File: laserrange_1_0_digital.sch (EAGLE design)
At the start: 32 parts, among them U1 STM32F10XRXT6

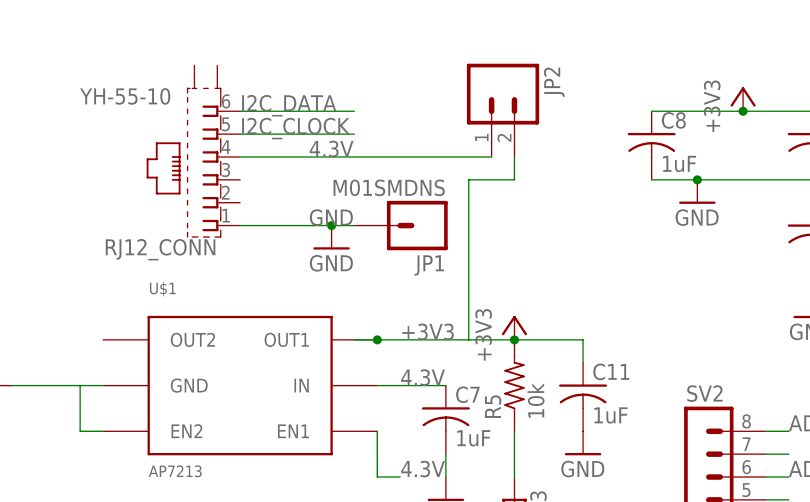
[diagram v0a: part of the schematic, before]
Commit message: Fixed the RJ12 connector footpad connections
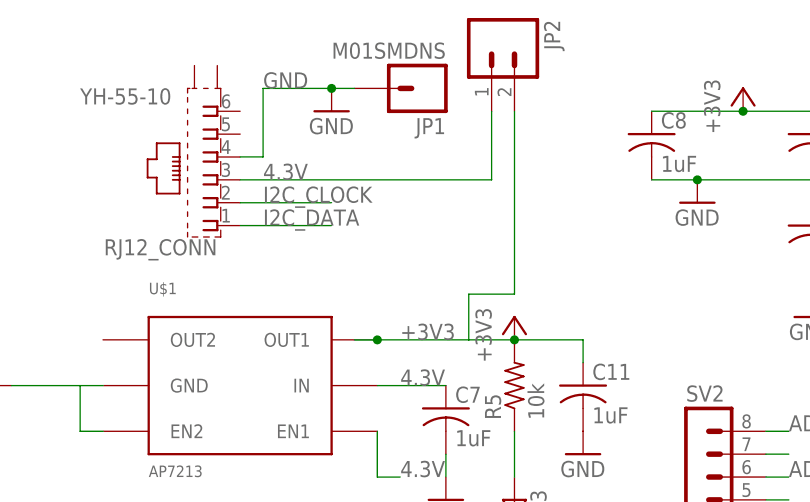
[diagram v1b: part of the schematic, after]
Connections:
- net 4.3V: now also RJ12_CONN.3; no longer RJ12_CONN.4
- net GND: now also RJ12_CONN.4; no longer RJ12_CONN.1
- net I2C_CLOCK: now also RJ12_CONN.2; no longer RJ12_CONN.5
- net I2C_DATA: now also RJ12_CONN.1; no longer RJ12_CONN.6
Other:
- moved on the sheet: JP1, JP2
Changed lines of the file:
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@@
 <instance part="GND6" gate="1" x="114.3" y="-25.4"/>
 <instance part="GND7" gate="1" x="25.4" y="55.88"/>
-<instance part="GND8" gate="1" x="-15.24" y="50.8"/>
+<instance part="GND8" gate="1" x="-15.24" y="66.04"/>
 <instance part="GND2" gate="1" x="5.08" y="0" rot="R90"/>
 <instance part="GND9" gate="1" x="53.34" y="66.04" rot="R270"/>
@@
 <instance part="R9" gate="G$1" x="157.48" y="-5.08"/>
 <instance part="GND15" gate="1" x="167.64" y="0"/>
-<instance part="JP2" gate="G$1" x="2.54" y="68.58" rot="R270"/>
-<instance part="JP1" gate="G$1" x="-5.08" y="53.34" rot="R180"/>
+<instance part="JP2" gate="G$1" x="2.54" y="73.66" rot="R270"/>
+<instance part="JP1" gate="G$1" x="-5.08" y="68.58" rot="R180"/>
 </instances>
 <busses>
@@
 <net name="4.3V" class="0">
 <segment>
-<label x="-17.78" y="60.96" size="1.778" layer="95"/>
-<pinref part="RJ12_CONN" gate="G$1" pin="4"/>
-<wire x1="2.54" y1="60.96" x2="-25.4" y2="60.96" width="0.1524" layer="91"/>
-<pinref part="JP2" gate="G$1" pin="1"/>
-</segment>
-<segment>
 <pinref part="U$1" gate="G$1" pin="IN"/>
 <wire x1="-10.16" y1="35.56" x2="-2.54" y2="35.56" width="0.1524" layer="91"/>
@@
 <label x="-7.62" y="25.4" size="1.778" layer="95"/>
 </segment>
+<segment>
+<pinref part="JP2" gate="G$1" pin="1"/>
+<wire x1="2.54" y1="66.04" x2="2.54" y2="58.42" width="0.1524" layer="91"/>
+<pinref part="RJ12_CONN" gate="G$1" pin="3"/>
+<wire x1="2.54" y1="58.42" x2="-25.4" y2="58.42" width="0.1524" layer="91"/>
+<label x="-22.86" y="58.42" size="1.778" layer="95"/>
+</segment>
 </net>
 <net name="I2C_CLOCK" class="0">
-<segment>
-<wire x1="-25.4" y1="63.5" x2="-12.7" y2="63.5" width="0.1524" layer="91"/>
-<label x="-25.4" y="63.5" size="1.778" layer="95"/>
-<pinref part="RJ12_CONN" gate="G$1" pin="5"/>
-</segment>
 <segment>
 <pinref part="U1" gate="PORTB_L" pin="PB6"/>
@@
 <label x="165.1" y="50.8" size="1.778" layer="95"/>
 </segment>
+<segment>
+<pinref part="RJ12_CONN" gate="G$1" pin="2"/>
+<wire x1="-25.4" y1="55.88" x2="-15.24" y2="55.88" width="0.1524" layer="91"/>
+<label x="-22.86" y="55.88" size="1.778" layer="95"/>
+</segment>
 </net>
 <net name="I2C_DATA" class="0">
-<segment>
-<wire x1="-25.4" y1="66.04" x2="-12.7" y2="66.04" width="0.1524" layer="91"/>
-<label x="-25.4" y="66.04" size="1.778" layer="95"/>
-<pinref part="RJ12_CONN" gate="G$1" pin="6"/>
-</segment>
 <segment>
 <pinref part="U1" gate="PORTB_L" pin="PB7"/>
@@
 <label x="165.1" y="58.42" size="1.778" layer="95"/>
 </segment>
+<segment>
+<pinref part="RJ12_CONN" gate="G$1" pin="1"/>
+<wire x1="-25.4" y1="53.34" x2="-15.24" y2="53.34" width="0.1524" layer="91"/>
+<label x="-22.86" y="53.34" size="1.778" layer="95"/>
+</segment>
 </net>
 <net name="GND" class="0">
 <segment>
-<wire x1="-25.4" y1="53.34" x2="-15.24" y2="53.34" width="0.1524" layer="91"/>
-<label x="-17.78" y="53.34" size="1.778" layer="95"/>
-<pinref part="RJ12_CONN" gate="G$1" pin="1"/>
+<label x="-22.86" y="68.58" size="1.778" layer="95"/>
 <pinref part="GND8" gate="1" pin="GND"/>
-<wire x1="-15.24" y1="53.34" x2="-12.7" y2="53.34" width="0.1524" layer="91"/>
-<junction x="-15.24" y="53.34"/>
 <pinref part="JP1" gate="G$1" pin="1"/>
+<wire x1="-15.24" y1="68.58" x2="-22.86" y2="68.58" width="0.1524" layer="91"/>
+<junction x="-15.24" y="68.58"/>
+<wire x1="-15.24" y1="68.58" x2="-12.7" y2="68.58" width="0.1524" layer="91"/>
+<pinref part="RJ12_CONN" gate="G$1" pin="4"/>
+<wire x1="-25.4" y1="60.96" x2="-22.86" y2="60.96" width="0.1524" layer="91"/>
+<wire x1="-22.86" y1="60.96" x2="-22.86" y2="68.58" width="0.1524" layer="91"/>
 </segment>
 <segment>
@@
 <wire x1="12.7" y1="40.64" x2="12.7" y2="38.1" width="0.1524" layer="91"/>
 <pinref part="JP2" gate="G$1" pin="2"/>
-<wire x1="5.08" y1="60.96" x2="5.08" y2="58.42" width="0.1524" layer="91"/>
-<wire x1="5.08" y1="58.42" x2="0" y2="58.42" width="0.1524" layer="91"/>
-<wire x1="0" y1="58.42" x2="0" y2="40.64" width="0.1524" layer="91"/>
-</segment>
-<segment>
+<wire x1="5.08" y1="66.04" x2="5.08" y2="45.72" width="0.1524" layer="91"/>
+<wire x1="5.08" y1="45.72" x2="0" y2="45.72" width="0.1524" layer="91"/>
+<wire x1="0" y1="45.72" x2="0" y2="40.64" width="0.1524" layer="91"/>
+</segment>
+<segment>
